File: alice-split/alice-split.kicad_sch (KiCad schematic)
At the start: 86 parts, among them J1 MJ-4PP-9-Lily58-cache-Lily58_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, J2 OLED-Lily58-cache, U1 Sparkfun_Pro_Micro

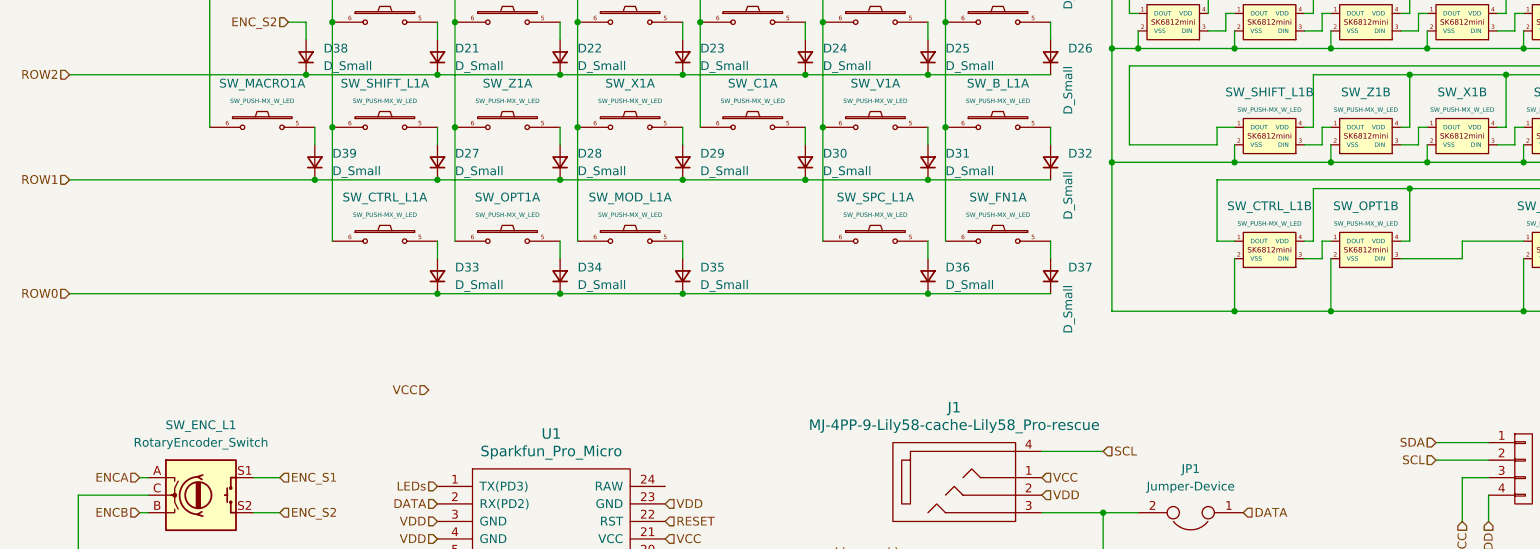
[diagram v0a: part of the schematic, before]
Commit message: Started trying to re-arrange the left hand side macro keys.
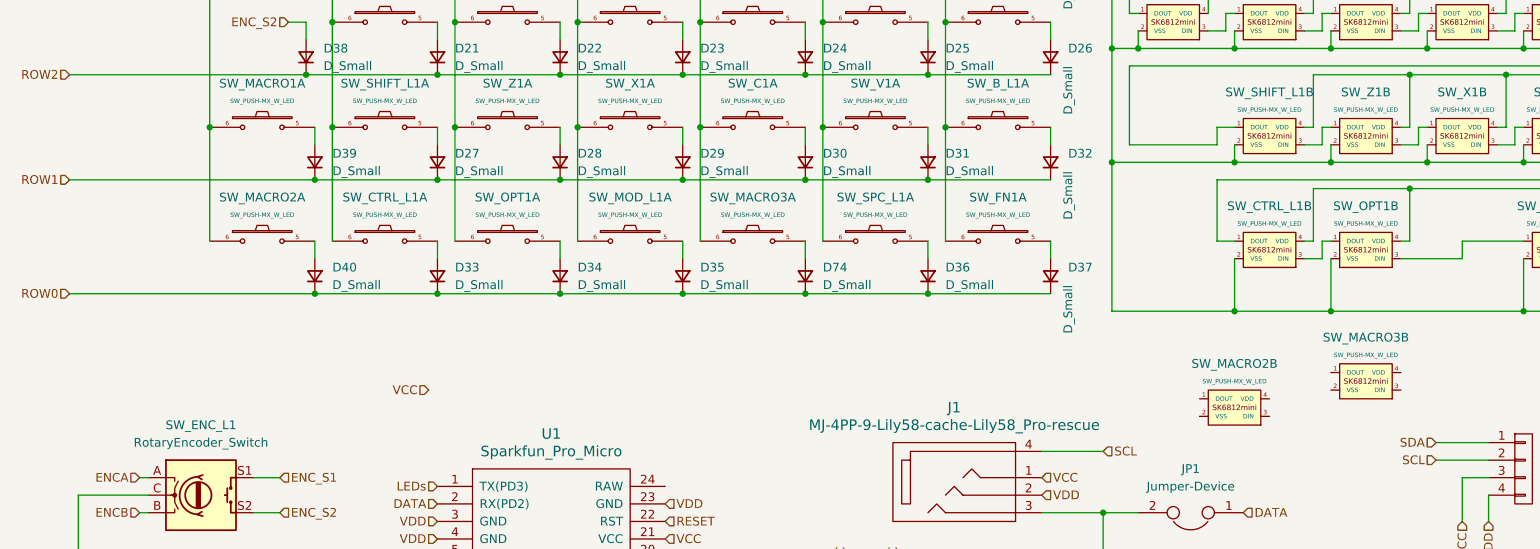
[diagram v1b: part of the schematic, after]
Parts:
- added D40, D74: D_Small, Diode_SMD:D_1206_3216Metric, symbol Device:D_Small
- added SW_MACRO2, SW_MACRO3: SW_PUSH-MX_W_LED, SofleRGB:SK6812MINI_and_cherry, symbol SofleKeyboard:SW_PUSH-MX_W_LED
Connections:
- net COL2: now also SW_MACRO3.6
- net COL6: now also SW_MACRO2.6
- net ROW0: now also D40.1 (K), D74.1 (K)
- new net: D74.2 (A), SW_MACRO3.5
- new net: D40.2 (A), SW_MACRO2.5

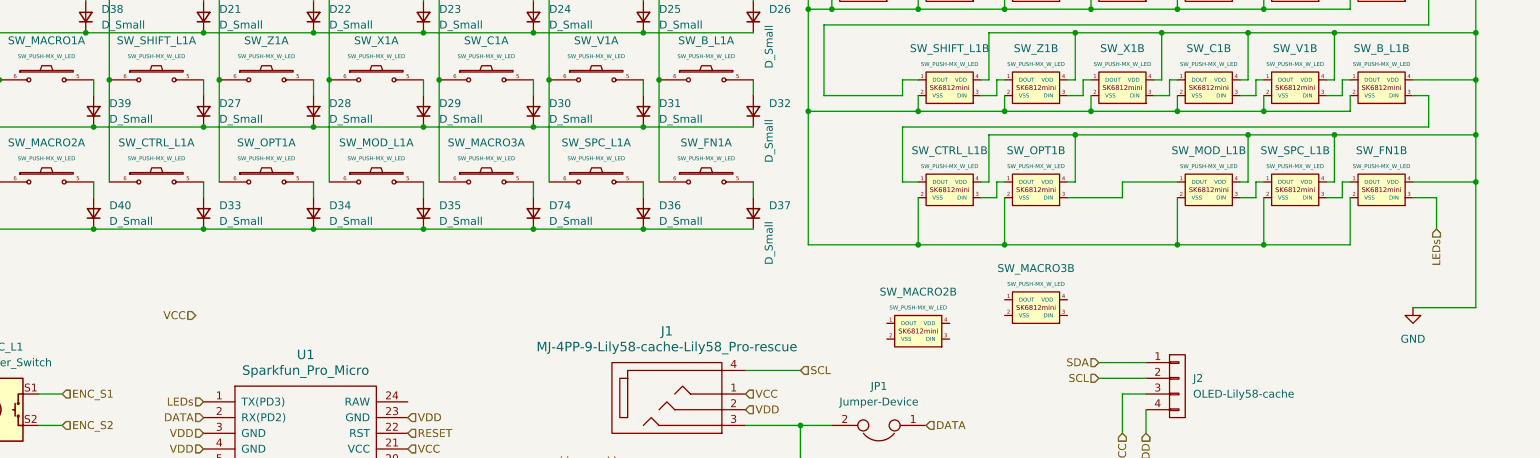
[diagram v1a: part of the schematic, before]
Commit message: Macro 2 and Macro 3 Placement
- Rearranged placement of macro 2 and macro 3 in the schematic.
- Started updating the wiring.
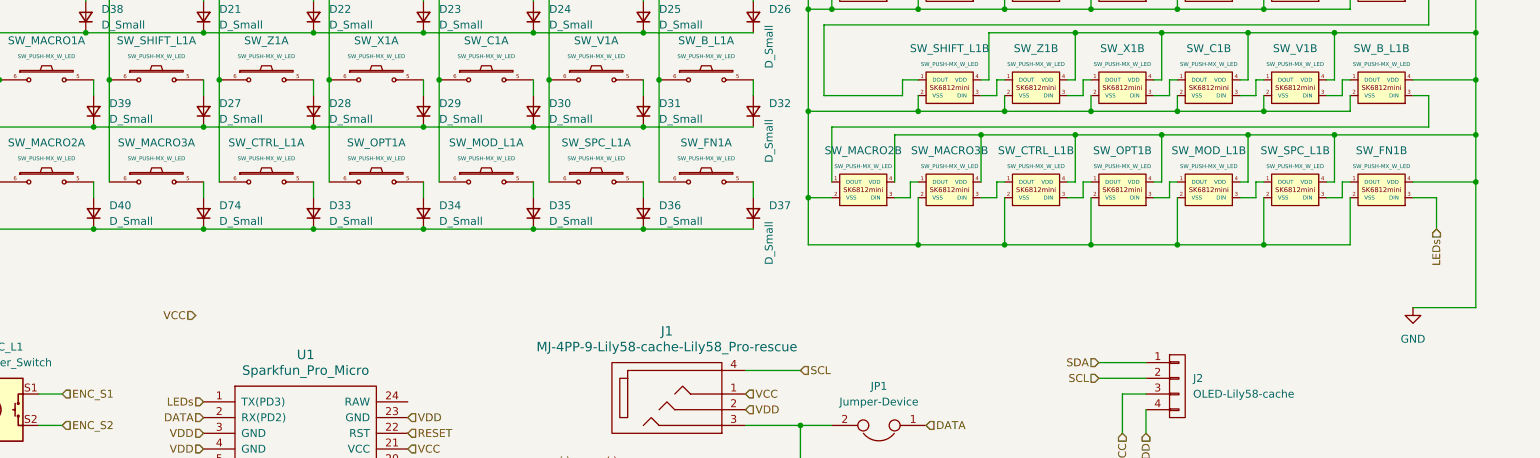
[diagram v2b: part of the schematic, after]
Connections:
- net COL2: now also SW_MOD_L1.6; no longer SW_MACRO3.6
- net COL3: now also SW_OPT1.6; no longer SW_MOD_L1.6
- net COL4: now also SW_CTRL_L1.6; no longer SW_OPT1.6
- net COL5: now also SW_MACRO3.6; no longer SW_CTRL_L1.6
- net GND: now also SW_MACRO2.4 (VDD), SW_MACRO3.4 (VDD)
- net VCC: now also SW_MACRO2.2 (VSS), SW_MACRO3.2 (VSS)
- net at SW_B_L1.3 (DIN): now also SW_MACRO2.1 (DOUT); no longer SW_CTRL_L1.1 (DOUT)
- net at SW_MACRO2.3 (DIN): now also SW_MACRO3.1 (DOUT)
- net at SW_MACRO3.3 (DIN): now also SW_CTRL_L1.1 (DOUT)
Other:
- moved on the sheet: D33, D34, D35, D74, SW_CTRL_L1A, SW_CTRL_L1B, SW_MACRO2B, SW_MACRO3A, SW_MACRO3B, SW_MOD_L1A, SW_OPT1A, SW_OPT1B
